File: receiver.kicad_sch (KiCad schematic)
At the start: 36 parts, among them J1 Screw_Terminal_01x02, J2 Screw_Terminal_01x02, Q1 BC549, Q2 BC549, U1 AMS1117-3.3

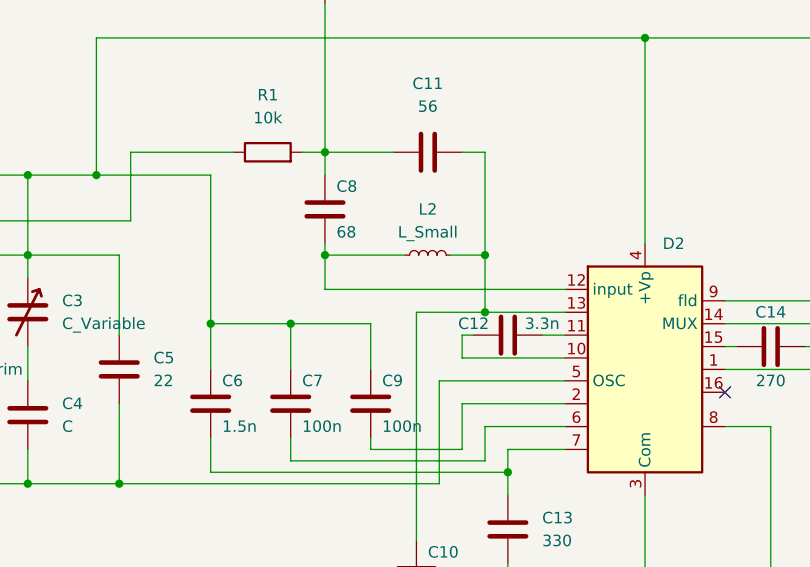
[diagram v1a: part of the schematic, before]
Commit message: Добавлена SMD-индуктивность.
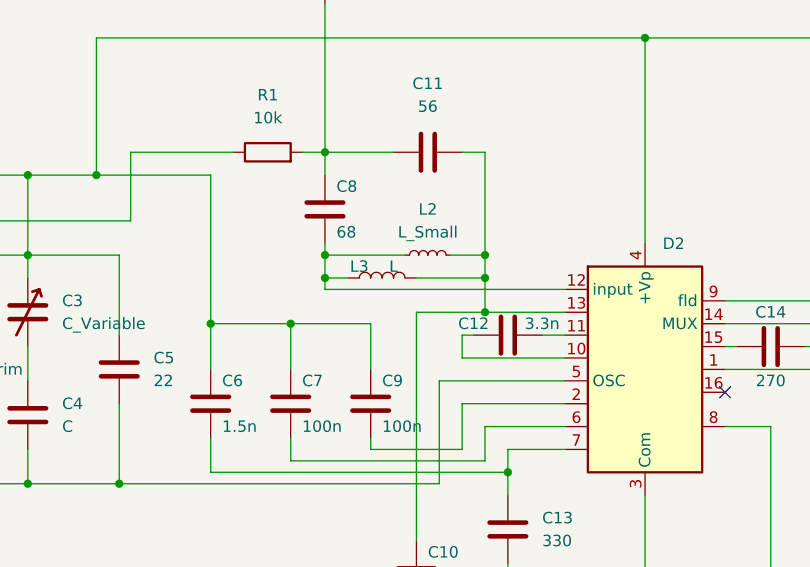
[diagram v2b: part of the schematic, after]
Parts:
- added L3: L, Inductor_SMD:L_1206_3216Metric_Pad1.22x1.90mm_HandSolder, symbol Device:L
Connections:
- net at C10.1, C11.2, D2.13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: now also L3.2
- net at C8.2, D2.12 (input), L2.1: now also L3.1
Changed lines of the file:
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@@
   (junction (at 101.6 87.63) (diameter 0) (color 0 0 0 0)
   )
+  (junction (at 152.4 90.17) (diameter 0) (color 0 0 0 0)
+  )
   (junction (at 93.98 133.35) (diameter 0) (color 0 0 0 0)
   )
   (junction (at 121.92 95.25) (diameter 0) (color 0 0 0 0)
+  )
+  (junction (at 134.62 90.17) (diameter 0) (color 0 0 0 0)
   )
   (junction (at 130.81 95.25) (diameter 0) (color 0 0 0 0)
@@
     (stroke (width 0) (type default))
   )
+  (wire (pts (xy 152.4 90.17) (xy 152.4 93.98))
+    (stroke (width 0) (type default))
+  )
   (wire (pts (xy 234.95 64.77) (xy 234.95 63.5))
     (stroke (width 0) (type default))
@@
     (stroke (width 0) (type default))
   )
+  (wire (pts (xy 144.78 90.17) (xy 152.4 90.17))
+    (stroke (width 0) (type default))
+  )
   (wire (pts (xy 154.94 111.76) (xy 154.94 114.3))
     (stroke (width 0) (type default))
@@
     (stroke (width 0) (type default))
   )
+  (wire (pts (xy 134.62 90.17) (xy 137.16 90.17))
+    (stroke (width 0) (type default))
+  )
   (wire (pts (xy 170.18 133.35) (xy 189.23 133.35))
     (stroke (width 0) (type default))
@@
     (stroke (width 0) (type default))
   )
-  (wire (pts (xy 152.4 87.63) (xy 152.4 93.98))
+  (wire (pts (xy 152.4 87.63) (xy 152.4 90.17))
     (stroke (width 0) (type default))
   )
@@
     (stroke (width 0) (type default))
   )
-  (wire (pts (xy 134.62 87.63) (xy 134.62 91.44))
+  (wire (pts (xy 134.62 87.63) (xy 134.62 90.17))
     (stroke (width 0) (type default))
   )
@@
   )
   (wire (pts (xy 149.86 109.22) (xy 149.86 104.14))
+    (stroke (width 0) (type default))
+  )
+  (wire (pts (xy 134.62 90.17) (xy 134.62 91.44))
     (stroke (width 0) (type default))
   )
@@
         )
       )
+    )
+  )
+  (symbol (lib_id "Device:L") (at 140.97 90.17 90) (unit 1)
+    (in_bom yes) (on_board yes) (dnp no)
+    (property "Reference" "L3" (at 138.43 88.9 90)
+      (effects (font (size 1.27 1.27)))
+    )
+    (property "Value" "L" (at 142.24 88.9 90)
+      (effects (font (size 1.27 1.27)))
+    )
+    (property "Footprint" "Inductor_SMD:L_1206_3216Metric_Pad1.22x1.90mm_HandSolder" (at 140.97 90.17 0)
+      (effects (font (size 1.27 1.27)) hide)
+    )
+    (property "Datasheet" "~" (at 140.97 90.17 0)
+      (effects (font (size 1.27 1.27)) hide)
+    )
+    (pin "1")
+    (pin "2")
+    (instances
+      (project "receiver"
+        (path "/4bdd428b-3ec4-4713-a3dd-c7716dea0b4d"
+          (reference "L3") (unit 1)
+        )
+      )

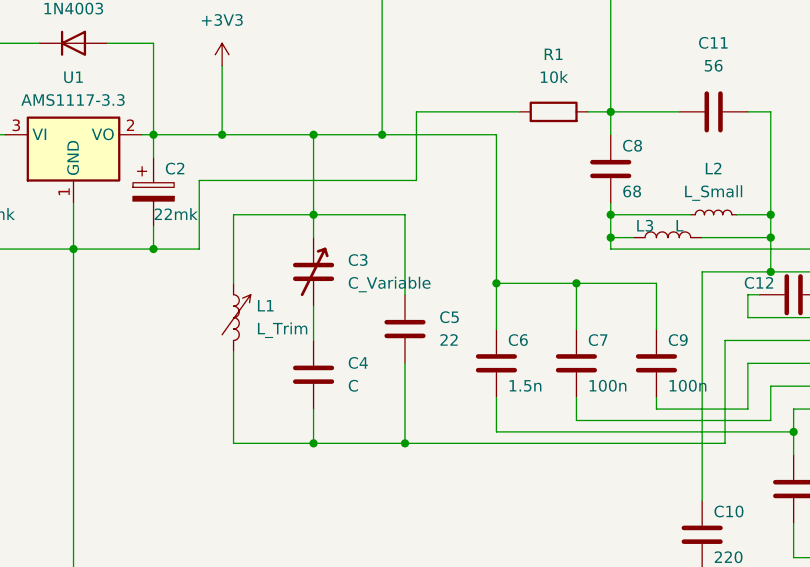
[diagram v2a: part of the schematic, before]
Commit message: Добавлено посадочное место для переменного конденсатора.
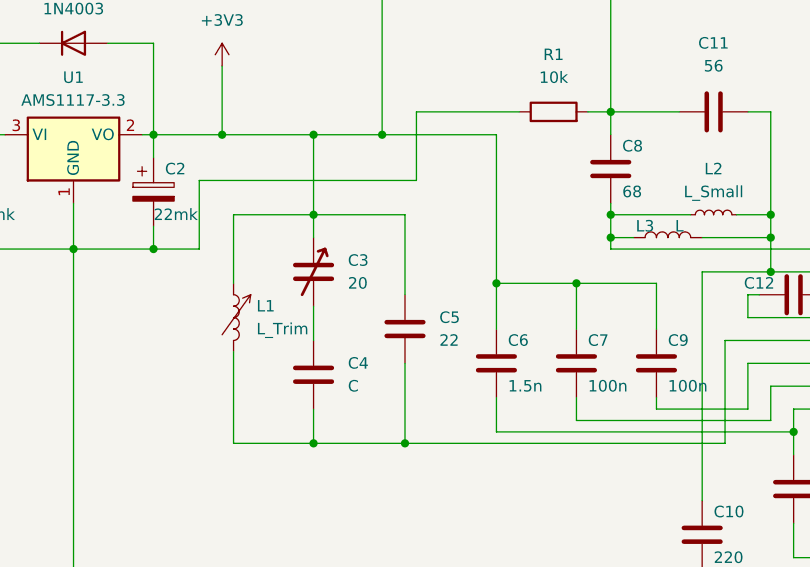
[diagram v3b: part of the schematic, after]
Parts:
- C17, C7, C9: footprint Capacitor_THT:C_Rect_L16.5mm_W4.7mm_P15.00mm_MKT -> Capacitor_THT:C_Axial_L5.1mm_D3.1mm_P15.00mm_Horizontal
- C3: value C_Variable -> 20; footprint (none) -> my_library:Capasitor_Variable
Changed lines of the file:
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@@
       (effects (font (size 1.27 1.27)) (justify left))
     )
-    (property "Value" "C_Variable" (at 105.41 95.25 0)
-      (effects (font (size 1.27 1.27)) (justify left))
-    )
-    (property "Footprint" "" (at 101.6 93.98 0)
+    (property "Value" "20" (at 105.41 95.25 0)
+      (effects (font (size 1.27 1.27)) (justify left))
+    )
+    (property "Footprint" "my_library:Capasitor_Variable" (at 101.6 93.98 0)
       (effects (font (size 1.27 1.27)) hide)
     )
@@
       (effects (font (size 1.27 1.27)) (justify left))
     )
-    (property "Footprint" "Capacitor_THT:C_Rect_L16.5mm_W4.7mm_P15.00mm_MKT" (at 140.6652 107.95 0)
+    (property "Footprint" "Capacitor_THT:C_Axial_L5.1mm_D3.1mm_P15.00mm_Horizontal" (at 140.6652 107.95 0)
       (effects (font (size 1.27 1.27)) hide)
     )
@@
       (effects (font (size 1.27 1.27)) (justify left))
     )
-    (property "Footprint" "Capacitor_THT:C_Rect_L16.5mm_W4.7mm_P15.00mm_MKT" (at 131.7752 107.95 0)
+    (property "Footprint" "Capacitor_THT:C_Axial_L5.1mm_D3.1mm_P15.00mm_Horizontal" (at 131.7752 107.95 0)
       (effects (font (size 1.27 1.27)) hide)
     )
@@
       (effects (font (size 1.27 1.27)) (justify left))
     )
-    (property "Footprint" "Capacitor_THT:C_Rect_L16.5mm_W4.7mm_P15.00mm_MKT" (at 202.8952 129.54 0)
-      (effects (font (size 1.27 1.27)) hide)
-    )
+    (property "Footprint" "Capacitor_THT:C_Axial_L5.1mm_D3.1mm_P15.00mm_Horizontal" (at 202.8952 129.54 0)
+      (effects (font (size 1.27 1.27)) hide)
+    )

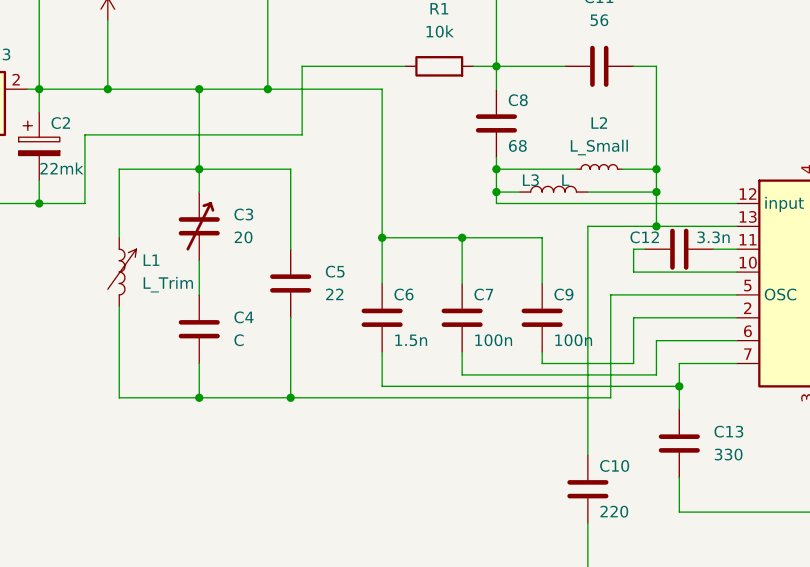
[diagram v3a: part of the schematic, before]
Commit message: посадочные места катушек индуктивности размещены по местам. вроде бы,все готово к производству.
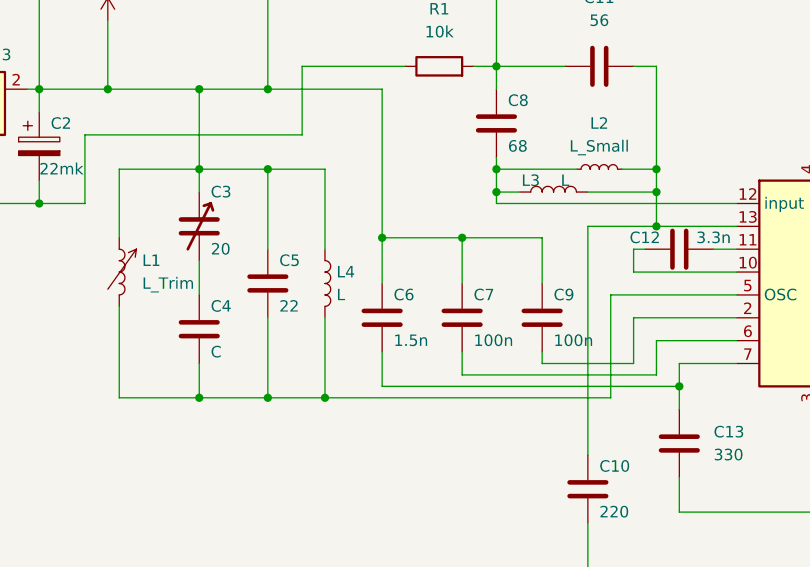
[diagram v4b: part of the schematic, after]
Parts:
- added L4: L, Inductor_SMD:L_1206_3216Metric_Pad1.22x1.90mm_HandSolder, symbol Device:L
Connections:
- net +3V3: now also L4.1
- net at C4.2, C5.2, D2.5 (OSC)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: now also L4.2
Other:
- moved on the sheet: C5
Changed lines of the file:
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@@
   (junction (at 62.23 78.74) (diameter 0) (color 0 0 0 0)
   )
+  (junction (at 115.57 113.03) (diameter 0) (color 0 0 0 0)
+  )
   (junction (at 189.23 133.35) (diameter 0) (color 0 0 0 0)
   )
@@
   (junction (at 170.18 133.35) (diameter 0) (color 0 0 0 0)
   )
-  (junction (at 111.76 113.03) (diameter 0) (color 0 0 0 0)
-  )
   (junction (at 154.94 111.76) (diameter 0) (color 0 0 0 0)
   )
@@
   (junction (at 130.81 95.25) (diameter 0) (color 0 0 0 0)
   )
+  (junction (at 109.22 113.03) (diameter 0) (color 0 0 0 0)
+  )
   (junction (at 201.93 88.9) (diameter 0) (color 0 0 0 0)
   )
@@
   )
   (junction (at 134.62 87.63) (diameter 0) (color 0 0 0 0)
+  )
+  (junction (at 109.22 87.63) (diameter 0) (color 0 0 0 0)
   )
   (junction (at 109.22 78.74) (diameter 0) (color 0 0 0 0)
@@
     (stroke (width 0) (type default))
   )
-  (wire (pts (xy 111.76 113.03) (xy 147.32 113.03))
-    (stroke (width 0) (type default))
-  )
   (wire (pts (xy 134.62 76.2) (xy 134.62 78.74))
     (stroke (width 0) (type default))
   )
+  (wire (pts (xy 101.6 87.63) (xy 109.22 87.63))
+    (stroke (width 0) (type default))
+  )
   (wire (pts (xy 222.25 133.35) (xy 222.25 110.49))
     (stroke (width 0) (type default))
@@
     (stroke (width 0) (type default))
   )
+  (wire (pts (xy 109.22 87.63) (xy 115.57 87.63))
+    (stroke (width 0) (type default))
+  )
   (wire (pts (xy 201.93 129.54) (xy 201.93 133.35))
     (stroke (width 0) (type default))
@@
     (stroke (width 0) (type default))
   )
+  (wire (pts (xy 115.57 104.14) (xy 115.57 113.03))
+    (stroke (width 0) (type default))
+  )
   (wire (pts (xy 222.25 76.2) (xy 222.25 78.74))
     (stroke (width 0) (type default))
@@
     (stroke (width 0) (type default))
   )
-  (wire (pts (xy 101.6 87.63) (xy 111.76 87.63))
-    (stroke (width 0) (type default))
-  )
   (wire (pts (xy 113.03 83.82) (xy 113.03 76.2))
     (stroke (width 0) (type default))
@@
     (stroke (width 0) (type default))
   )
-  (wire (pts (xy 111.76 113.03) (xy 111.76 104.14))
-    (stroke (width 0) (type default))
-  )
   (wire (pts (xy 189.23 92.71) (xy 189.23 121.92))
     (stroke (width 0) (type default))
@@
     (stroke (width 0) (type default))
   )
-  (wire (pts (xy 101.6 113.03) (xy 111.76 113.03))
+  (wire (pts (xy 101.6 113.03) (xy 109.22 113.03))
     (stroke (width 0) (type default))
   )
@@
     (stroke (width 0) (type default))
   )
+  (wire (pts (xy 109.22 113.03) (xy 115.57 113.03))
+    (stroke (width 0) (type default))
+  )
   (wire (pts (xy 71.12 68.58) (xy 62.23 68.58))
     (stroke (width 0) (type default))
@@
     (stroke (width 0) (type default))
   )
+  (wire (pts (xy 115.57 87.63) (xy 115.57 96.52))
+    (stroke (width 0) (type default))
+  )
   (wire (pts (xy 219.71 114.3) (xy 226.06 114.3))
     (stroke (width 0) (type default))
@@
     (stroke (width 0) (type default))
   )
+  (wire (pts (xy 115.57 113.03) (xy 147.32 113.03))
+    (stroke (width 0) (type default))
+  )
   (wire (pts (xy 62.23 68.58) (xy 62.23 78.74))
     (stroke (width 0) (type default))
   )
+  (wire (pts (xy 109.22 104.14) (xy 109.22 113.03))
+    (stroke (width 0) (type default))
+  )
   (wire (pts (xy 144.78 93.98) (xy 152.4 93.98))
     (stroke (width 0) (type default))
@@
     (stroke (width 0) (type default))
   )
-  (wire (pts (xy 111.76 87.63) (xy 111.76 96.52))
-    (stroke (width 0) (type default))
-  )
   (wire (pts (xy 113.03 76.2) (xy 124.46 76.2))
     (stroke (width 0) (type default))
@@
   )
   (wire (pts (xy 121.92 95.25) (xy 130.81 95.25))
+    (stroke (width 0) (type default))
+  )
+  (wire (pts (xy 109.22 87.63) (xy 109.22 96.52))
     (stroke (width 0) (type default))
   )
@@
     )
   )
-  (symbol (lib_id "Device:C") (at 111.76 100.33 0) (unit 1)
-    (in_bom yes) (on_board yes) (dnp no) (fields_autoplaced)
-    (property "Reference" "C5" (at 115.57 99.06 0)
-      (effects (font (size 1.27 1.27)) (justify left))
-    )
-    (property "Value" "22" (at 115.57 101.6 0)
-      (effects (font (size 1.27 1.27)) (justify left))
-    )
-    (property "Footprint" "Capacitor_THT:C_Rect_L11.0mm_W2.8mm_P10.00mm_MKT" (at 112.7252 104.14 0)
-      (effects (font (size 1.27 1.27)) hide)
-    )
-    (property "Datasheet" "~" (at 111.76 100.33 0)
+  (symbol (lib_id "Device:C") (at 109.22 100.33 0) (unit 1)
+    (in_bom yes) (on_board yes) (dnp no)
+    (property "Reference" "C5" (at 110.49 97.79 0)
+      (effects (font (size 1.27 1.27)) (justify left))
+    )
+    (property "Value" "22" (at 110.49 102.87 0)
+      (effects (font (size 1.27 1.27)) (justify left))
+    )
+    (property "Footprint" "Capacitor_THT:C_Rect_L11.0mm_W2.8mm_P10.00mm_MKT" (at 110.1852 104.14 0)
+      (effects (font (size 1.27 1.27)) hide)
+    )
+    (property "Datasheet" "~" (at 109.22 100.33 0)
       (effects (font (size 1.27 1.27)) hide)
     )
@@
   )
   (symbol (lib_id "Device:C_Variable") (at 101.6 93.98 0) (unit 1)
-    (in_bom yes) (on_board yes) (dnp no) (fields_autoplaced)
-    (property "Reference" "C3" (at 105.41 92.71 0)
-      (effects (font (size 1.27 1.27)) (justify left))
-    )
-    (property "Value" "20" (at 105.41 95.25 0)
+    (in_bom yes) (on_board yes) (dnp no)
+    (property "Reference" "C3" (at 102.87 90.17 0)
+      (effects (font (size 1.27 1.27)) (justify left))
+    )
+    (property "Value" "20" (at 102.87 96.52 0)
       (effects (font (size 1.27 1.27)) (justify left))
     )
@@
   )
   (symbol (lib_id "Device:C") (at 101.6 105.41 0) (unit 1)
-    (in_bom yes) (on_board yes) (dnp no) (fields_autoplaced)
-    (property "Reference" "C4" (at 105.41 104.14 0)
-      (effects (font (size 1.27 1.27)) (justify left))
-    )
-    (property "Value" "C" (at 105.41 106.68 0)
+    (in_bom yes) (on_board yes) (dnp no)
+    (property "Reference" "C4" (at 102.87 102.87 0)
+      (effects (font (size 1.27 1.27)) (justify left))
+    )
+    (property "Value" "C" (at 102.87 107.95 0)
       (effects (font (size 1.27 1.27)) (justify left))
     )
@@
         )
       )
+    )
+  )
+  (symbol (lib_id "Device:L") (at 115.57 100.33 0) (unit 1)
+    (in_bom yes) (on_board yes) (dnp no) (fields_autoplaced)
+    (property "Reference" "L4" (at 116.84 99.06 0)
+      (effects (font (size 1.27 1.27)) (justify left))
+    )
+    (property "Value" "L" (at 116.84 101.6 0)
+      (effects (font (size 1.27 1.27)) (justify left))
+    )
+    (property "Footprint" "Inductor_SMD:L_1206_3216Metric_Pad1.22x1.90mm_HandSolder" (at 115.57 100.33 0)
+      (effects (font (size 1.27 1.27)) hide)
+    )
+    (property "Datasheet" "~" (at 115.57 100.33 0)
+      (effects (font (size 1.27 1.27)) hide)
+    )
+    (pin "1")
+    (pin "2")
+    (instances
+      (project "receiver"
+        (path "/4bdd428b-3ec4-4713-a3dd-c7716dea0b4d"
+          (reference "L4") (unit 1)
+        )
+      )
